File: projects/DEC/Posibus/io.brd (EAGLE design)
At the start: 177.8 x 127 mm, 11 parts

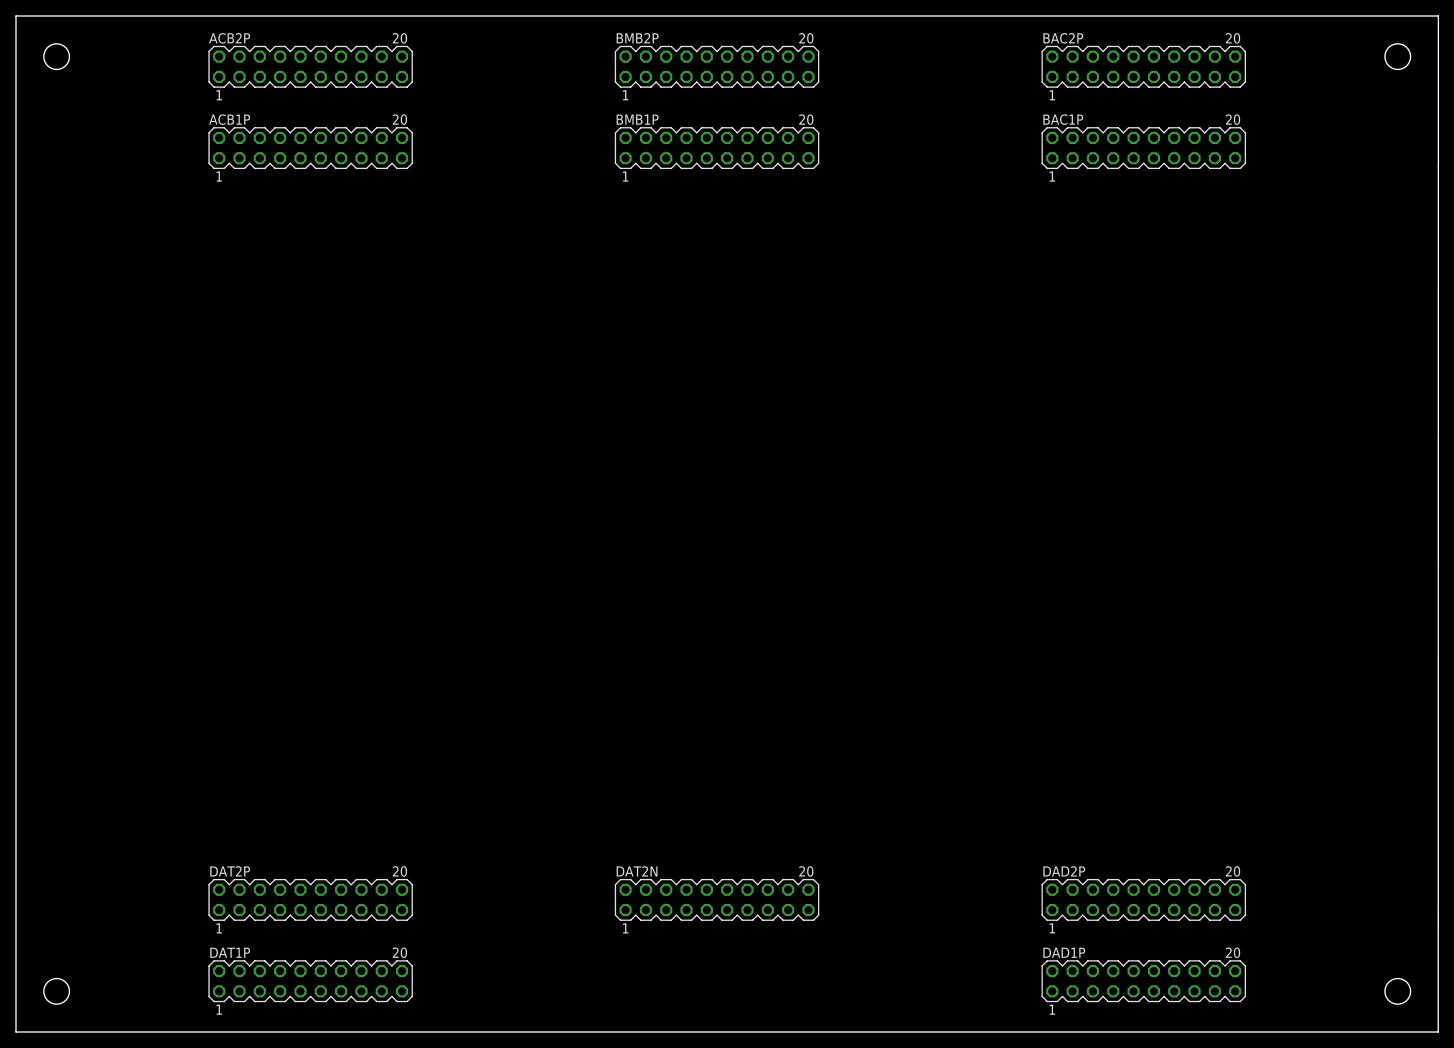
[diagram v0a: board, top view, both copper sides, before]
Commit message: Fix mounting hole sizes in Posibus project for #6 fasteners.
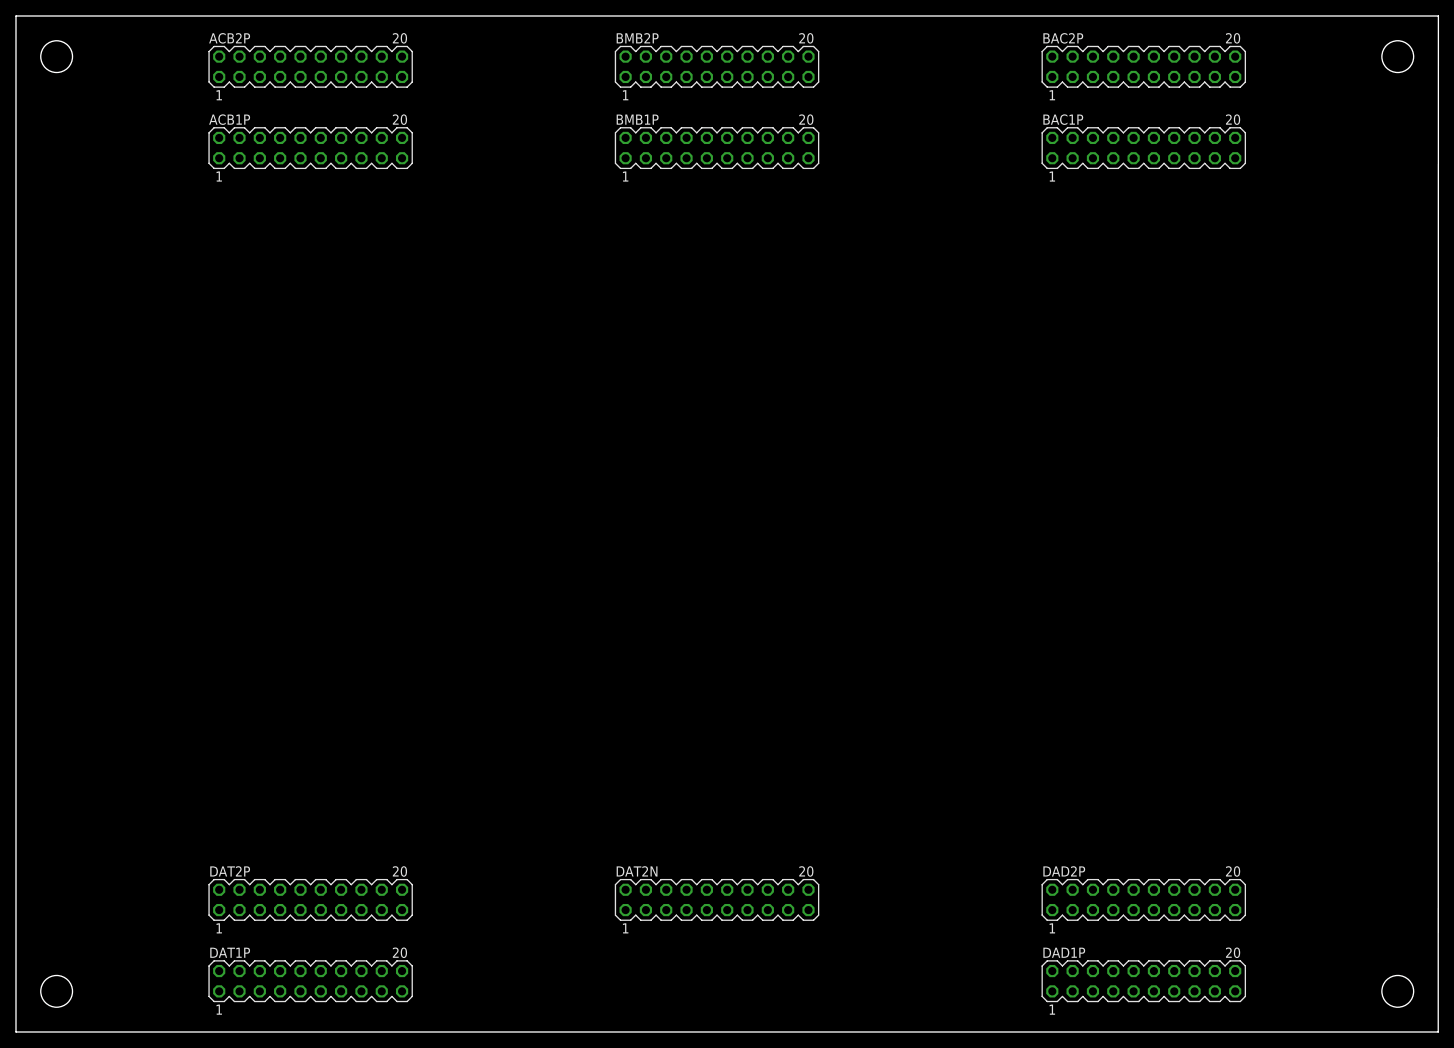
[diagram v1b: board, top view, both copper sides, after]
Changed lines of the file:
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@@
 <wire x1="177.8" y1="127" x2="0" y2="127" width="0" layer="20"/>
 <wire x1="0" y1="127" x2="0" y2="0" width="0" layer="20"/>
-<hole x="5.08" y="121.92" drill="3.2"/>
-<hole x="172.72" y="121.92" drill="3.2"/>
-<hole x="172.72" y="5.08" drill="3.2"/>
-<hole x="5.08" y="5.08" drill="3.2"/>
+<hole x="5.08" y="121.92" drill="3.96875"/>
+<hole x="172.72" y="121.92" drill="3.96875"/>
+<hole x="172.72" y="5.08" drill="3.96875"/>
+<hole x="5.08" y="5.08" drill="3.96875"/>
 </plain>
 <attributes>
